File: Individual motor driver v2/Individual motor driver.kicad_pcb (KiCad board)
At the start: 2 copper layers, 99.9 x 99.9 mm, 46 parts, among them P1 CONN_01X06, P2 CONN_01X01, P3 CONN_01X02, P4 CONN_01X06, P5 CONN_01X02, P6 CONN_01X02, P7 CONN_01X01, P9 CONN_01X02, Q1 PN2222A, Q2 PN2222A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

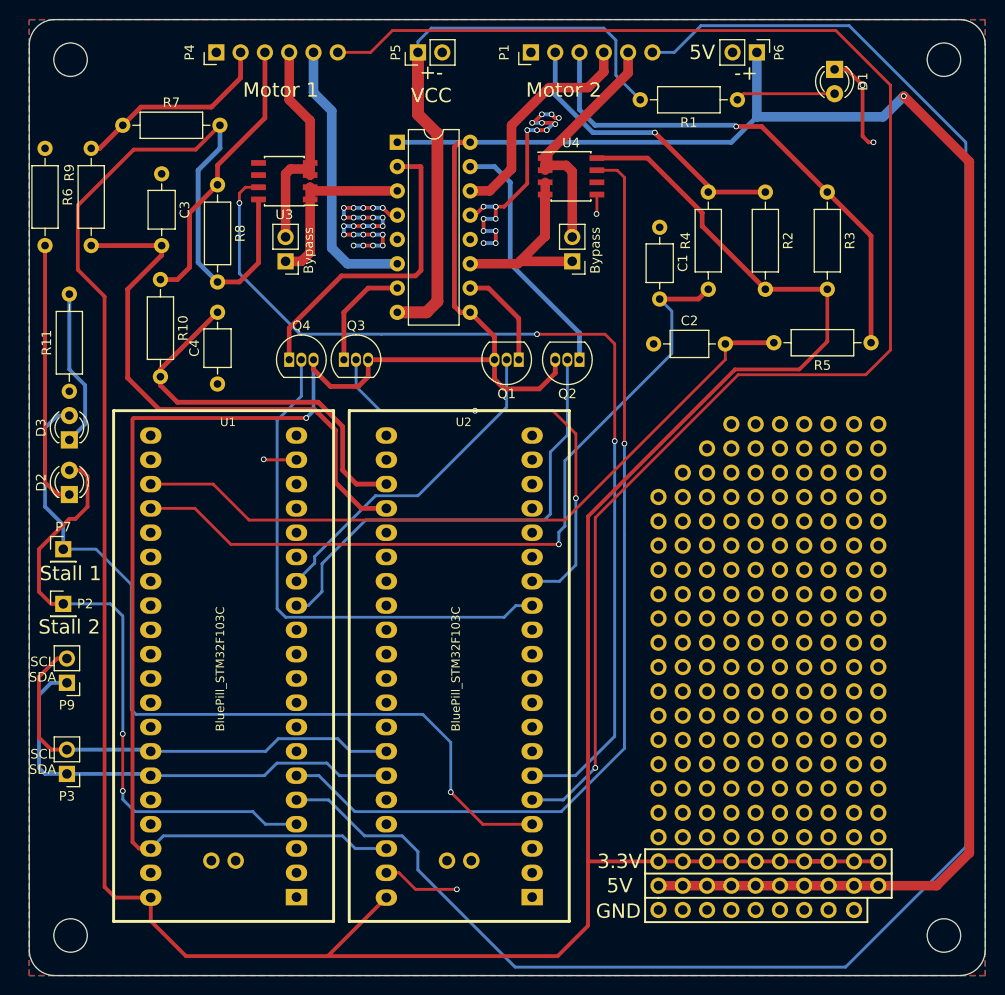
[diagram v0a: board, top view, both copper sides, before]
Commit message: Made small changes to the V2 board and regenerated gerbers
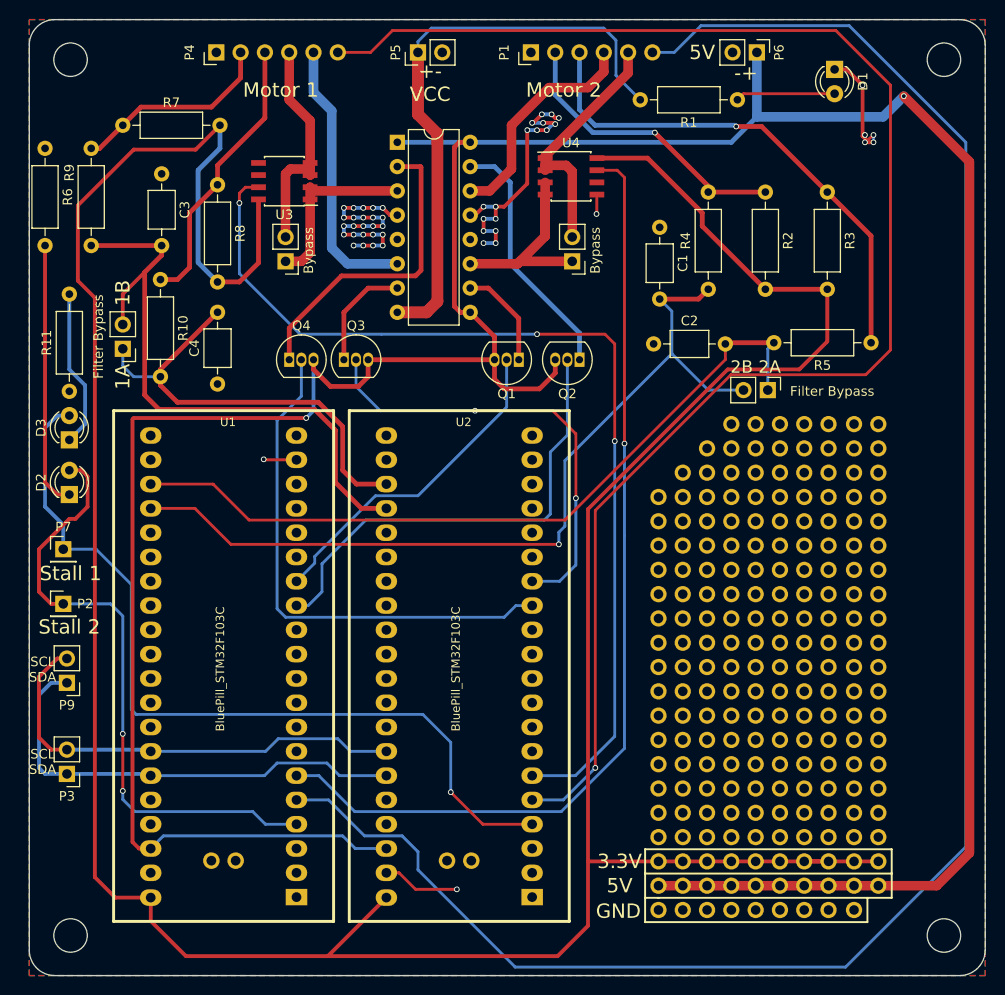
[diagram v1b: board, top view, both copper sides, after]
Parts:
- added REF**: PinHeader_1x02_P2.54mm_Vertical, Connector_PinHeader_2.54mm:PinHeader_1x02_P2.54mm_Vertical, F.Cu at (159.4, 76.7)
- added REF**: PinHeader_1x02_P2.54mm_Vertical, Connector_PinHeader_2.54mm:PinHeader_1x02_P2.54mm_Vertical, F.Cu at (91.9, 72.4)
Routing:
- net Rotary_Encoder_2B: track 80.8 -> 89.9 mm
- net Rotary_Encoder_1A: track 40.7 -> 46.9 mm
- net Rotary_Encoder_2A: track 75.4 -> 80.6 mm
- net Rotary_Encoder_1B: track 58.6 -> 63.5 mm
- net GND: track 78.5 -> 81.2 mm, vias 46 -> 49
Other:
- board text added: "1A"
- board text added: "1B"
- board text added: "2B 2A"
- board text added: "Filter Bypass"
